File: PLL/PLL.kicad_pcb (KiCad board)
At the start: 2 copper layers, 50 x 200 mm, 81 parts, among them J1 Clock, J10 Mix, J2 EuroPower, J3 D8, J4 D4, J5 D2, J6 M1, J7 M2, J8 M4, J9 M8, SW1 Lock speed, U1 TL082, U2 CD4046, U3 CD4040

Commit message: PLL done
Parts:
- R1, R2: footprint Resistor_SMD:R_1206_3216Metric_Pad1.42x1.75mm_HandSolder -> Resistor_THT:R_Axial_DIN0204_L3.6mm_D1.6mm_P7.62mm_Horizontal
- R7: moved to B.Cu
- moved R7 70.5 mm to (32.3, 33.2), turned to 90 degrees
- moved R2 66.2 mm to (54.6, 25.2), turned to 315 degrees
- moved R1 55.3 mm to (28.4, 53.7), turned to 180 degrees
- moved R19 10.7 mm to (22.0, 83.7), turned to 180 degrees
- moved R22 10.7 mm to (22.0, 143.7), turned to 180 degrees
- moved R23 10.7 mm to (22.0, 163.7), turned to 180 degrees
- moved R20 10.6 mm to (21.9, 103.7), turned to 180 degrees
- moved R24 10.6 mm to (22.0, 183.6), turned to 180 degrees
- moved R21 10.6 mm to (22.0, 123.6), turned to 180 degrees
- moved R25 10.6 mm to (21.9, 203.7), turned to 180 degrees
- moved RV7 9.79 mm to (26.8, 194.5), turned to 270 degrees
- moved RV6 8.40 mm to (26.8, 174.4), turned to 270 degrees
- moved RV5 6.58 mm to (26.8, 154.5), turned to 270 degrees
- moved RV4 4.24 mm to (26.8, 134.5), turned to 270 degrees
- moved R9 4.20 mm to (38.8, 44.9), turned to 90 degrees
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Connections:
- R2 pad 1: Net-(J1-PadRN) -> +12V
- R2 pad 2: +12V -> Net-(J1-PadRN)
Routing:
- net /Reset: track 0.00 -> 48.1 mm
- net /Clk_in: track 51.7 -> 13.8 mm
- net /Trig: track 2.33 -> 30.8 mm, vias 0 -> 1
- net Net-(R21-Pad1): track 39.4 -> 12.2 mm
- net Net-(R20-Pad1): track 38.9 -> 12.2 mm
- net Net-(R22-Pad1): track 38.8 -> 12.2 mm
- net Net-(R16-Pad1): track 19.4 -> 0.00 mm
- net Net-(R19-Pad2): track 208.4 -> 225.9 mm
- net +12V: track 86.9 -> 102.5 mm
- net Net-(R19-Pad1): track 0.00 -> 12.2 mm
- net Net-(R25-Pad1): track 0.00 -> 12.2 mm
- net Net-(R24-Pad1): track 0.00 -> 12.2 mm
- net Net-(R23-Pad1): track 0.00 -> 12.2 mm
- net Net-(C8-Pad2): track 7.59 -> 18.7 mm
- net Net-(C10-Pad2): track 7.59 -> 18.7 mm
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
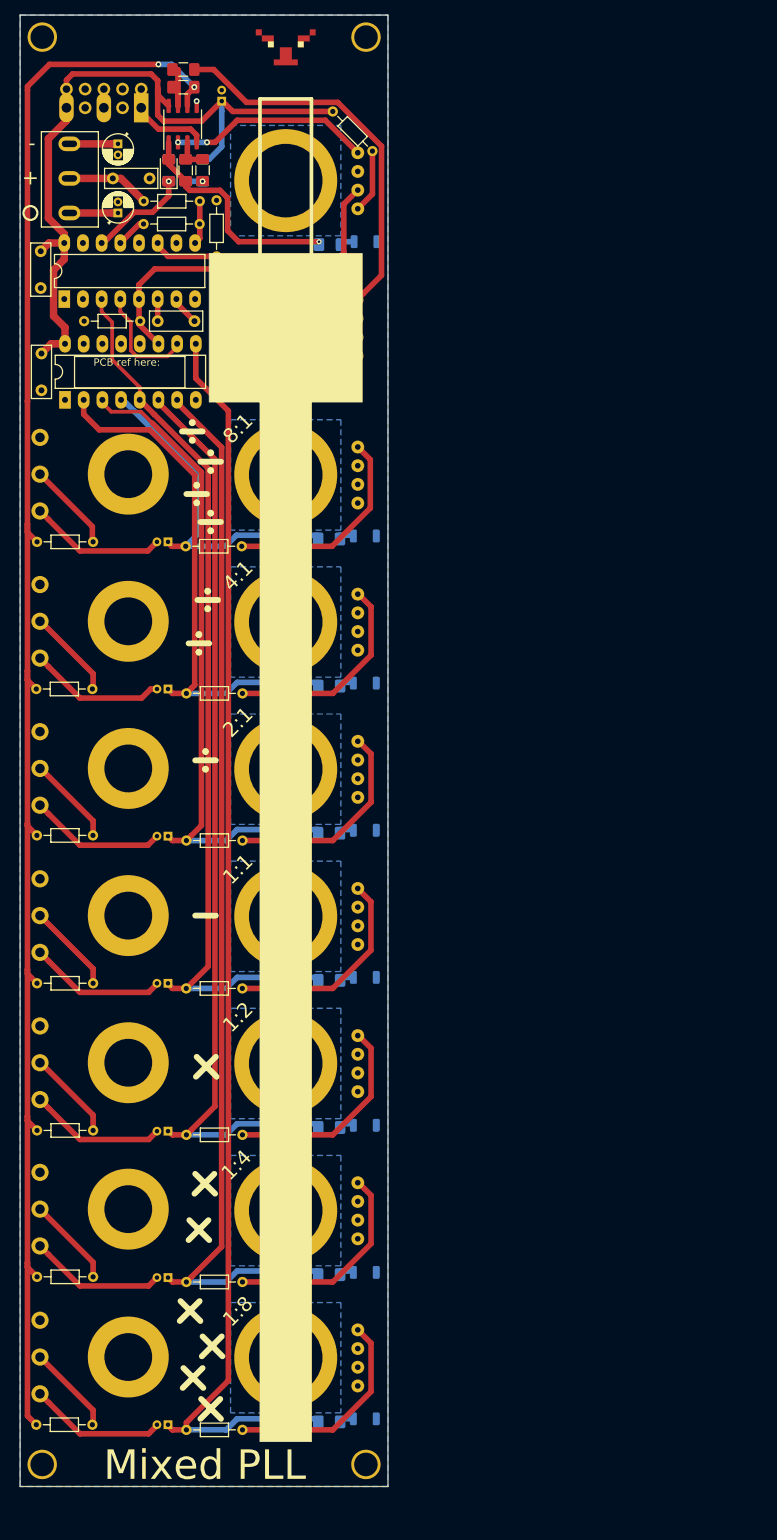
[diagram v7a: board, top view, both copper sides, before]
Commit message: More clearance
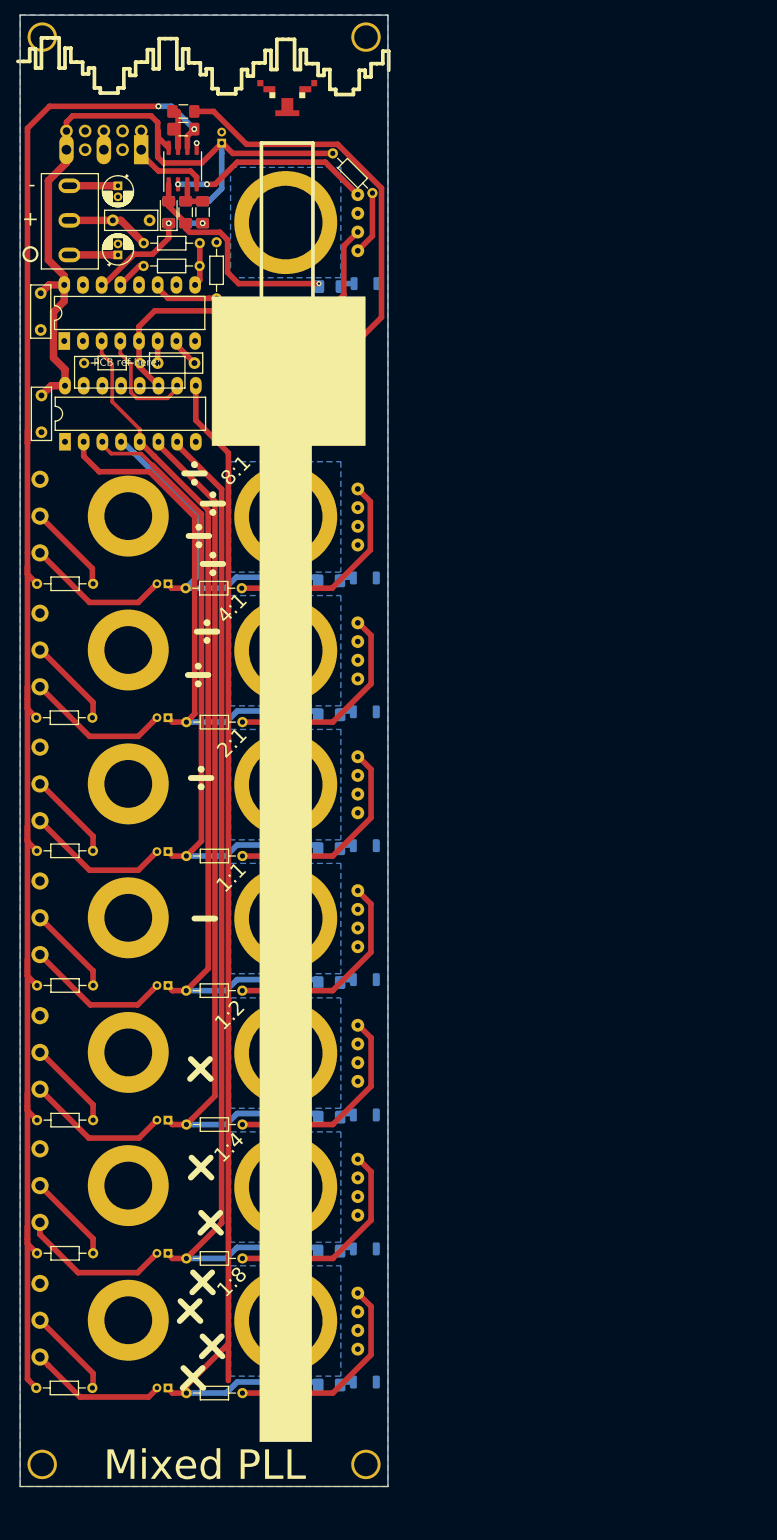
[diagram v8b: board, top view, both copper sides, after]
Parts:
- moved LOGO1 6.90 mm to (48.4, 25.0)
- moved C5 5.70 mm to (29.7, 40.0)
- moved C6 5.70 mm to (25.4, 44.7)
- moved C8 5.70 mm to (32.2, 89.4)
- moved D1 5.70 mm to (32.3, 38.9)
- moved D2 5.70 mm to (59.0, 48.6)
- moved J3 5.70 mm to (48.2, 80.3)
- moved R10 5.70 mm to (54.1, 89.0)
- moved R15 5.70 mm to (28.9, 46.2)
- moved R16 5.70 mm to (36.5, 43.1)
- moved R19 5.70 mm to (22.0, 89.4)
- moved R26 5.70 mm to (34.3, 27.6)
- moved R28 5.70 mm to (42.2, 90.0)
- moved R5 5.70 mm to (36.9, 38.9)
- moved R7 5.70 mm to (32.3, 38.9)
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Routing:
- net /M4: track 145.7 -> 136.8 mm
- net /M2: track 126.0 -> 118.9 mm
- net /M8: track 173.1 -> 167.4 mm
- net /M1: track 122.6 -> 117.2 mm
- net /D2: track 90.0 -> 86.4 mm
- net Net-(C13-Pad2): track 18.6 -> 20.8 mm
- net /D4: track 71.9 -> 70.1 mm
- net Net-(C11-Pad2): track 18.6 -> 19.8 mm
- net Net-(C9-Pad2): track 18.7 -> 19.7 mm
- net Net-(C8-Pad2): track 18.7 -> 19.7 mm
- net Net-(C10-Pad2): track 18.7 -> 19.7 mm
- net Net-(C12-Pad2): track 18.6 -> 19.7 mm
